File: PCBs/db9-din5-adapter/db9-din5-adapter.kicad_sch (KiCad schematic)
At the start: 4 parts, among them J1 DB25_Plug_MountingHoles, J2 TX/RX Straight/cross, J3 DTR/RTS Straight/cross

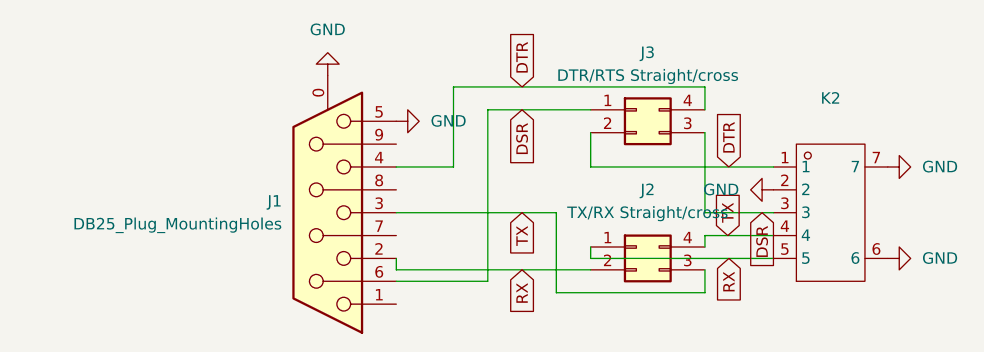
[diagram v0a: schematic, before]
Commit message: Update Quicktake doc and PCBs
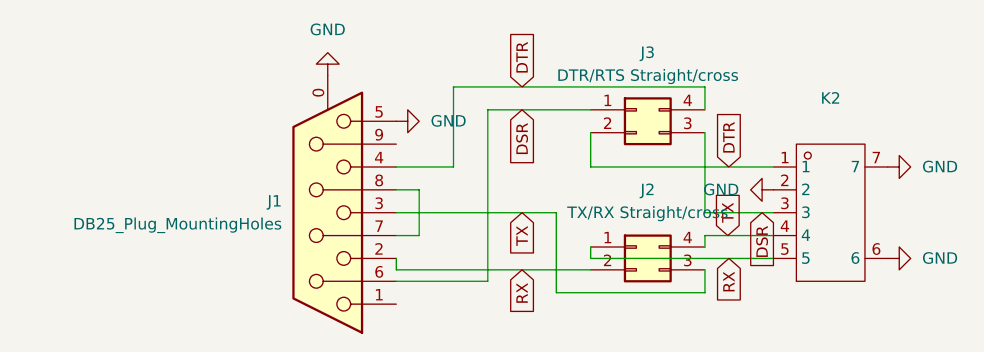
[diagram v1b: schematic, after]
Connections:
- net at J1.7: now also J1.8
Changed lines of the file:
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@@
+	(wire
+		(pts
+			(xy 107.95 74.93) (xy 110.49 74.93)
+		)
+		(stroke
+			(width 0)
+			(type default)
+		)
+	)
 	(wire
 		(pts
@@
 	(wire
 		(pts
+			(xy 110.49 69.85) (xy 107.95 69.85)
+		)
+		(stroke
+			(width 0)
+			(type default)
+		)
+	)
+	(wire
+		(pts
 			(xy 142.24 76.2) (xy 142.24 74.93)
 		)
@@
 		(pts
 			(xy 129.54 76.2) (xy 129.54 77.47)
+		)
+		(stroke
+			(width 0)
+			(type default)
+		)
+	)
+	(wire
+		(pts
+			(xy 110.49 74.93) (xy 110.49 69.85)
 		)
 		(stroke
@@
 		)
 		(instances
-			(project "db25-din5-adapter"
+			(project "db9-din5-adapter"
 				(path "/7108ec36-da4c-4f22-b5ad-0a42d2aa000b"
 					(reference "J3")
@@
 		)
 		(instances
-			(project ""
+			(project "db9-din5-adapter"
 				(path "/7108ec36-da4c-4f22-b5ad-0a42d2aa000b"
 					(reference "J1")
@@
 		)
 		(instances
-			(project "db25-din5-adapter"
+			(project "db9-din5-adapter"
 				(path "/7108ec36-da4c-4f22-b5ad-0a42d2aa000b"
 					(reference "#PWR04")
@@
 		)
 		(instances
-			(project "db25-din5-adapter"
+			(project "db9-din5-adapter"
 				(path "/7108ec36-da4c-4f22-b5ad-0a42d2aa000b"
 					(reference "#PWR01")
@@
 		)
 		(instances
-			(project "db25-din5-adapter"
+			(project "db9-din5-adapter"
 				(path "/7108ec36-da4c-4f22-b5ad-0a42d2aa000b"
 					(reference "K2")
@@
 		)
 		(instances
-			(project "db25-din5-adapter"
+			(project "db9-din5-adapter"
 				(path "/7108ec36-da4c-4f22-b5ad-0a42d2aa000b"
 					(reference "#PWR03")
@@
 		)
 		(instances
-			(project "db25-din5-adapter"
+			(project "db9-din5-adapter"
 				(path "/7108ec36-da4c-4f22-b5ad-0a42d2aa000b"
 					(reference "J2")
@@
 		)
 		(instances
-			(project "db25-din5-adapter"
+			(project "db9-din5-adapter"
 				(path "/7108ec36-da4c-4f22-b5ad-0a42d2aa000b"
 					(reference "#PWR02")
